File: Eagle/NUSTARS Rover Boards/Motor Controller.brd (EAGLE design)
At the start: 53.3 x 59.7 mm, 15 parts

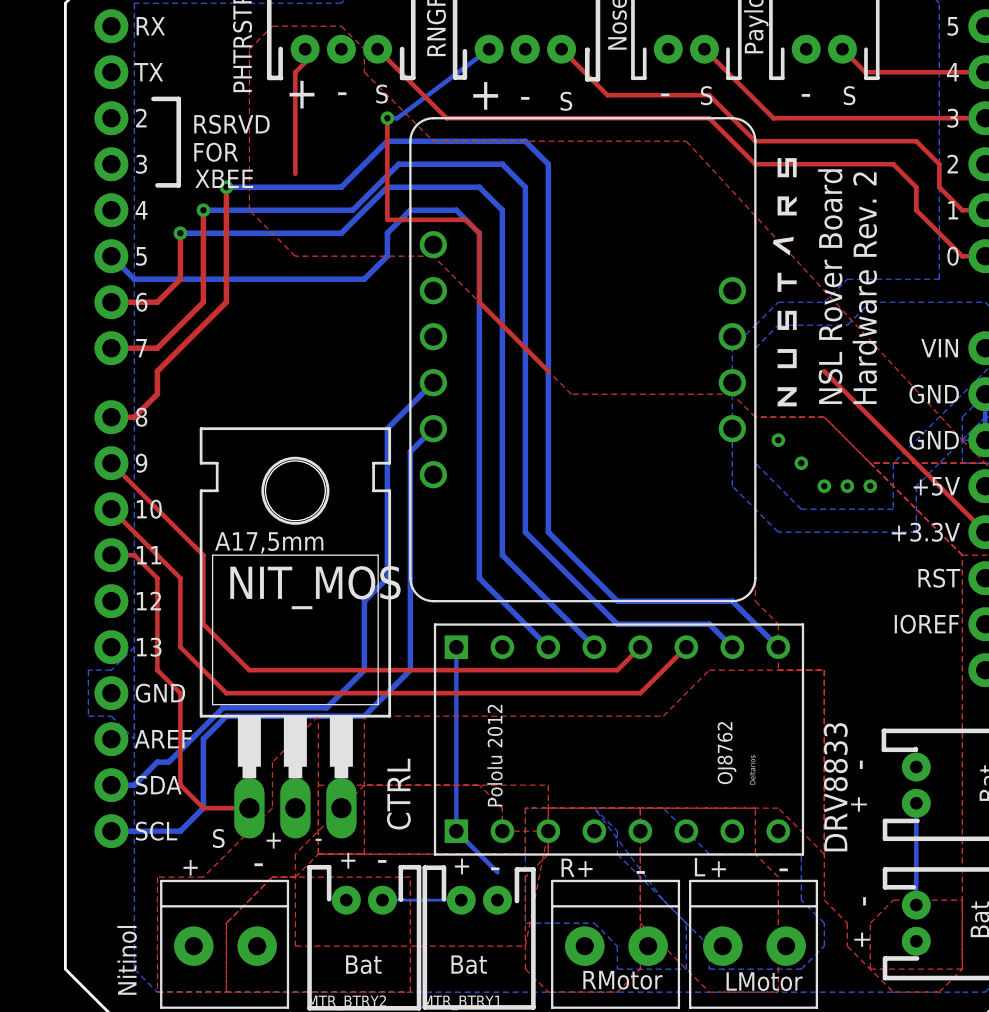
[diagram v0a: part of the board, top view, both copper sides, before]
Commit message: Add rover
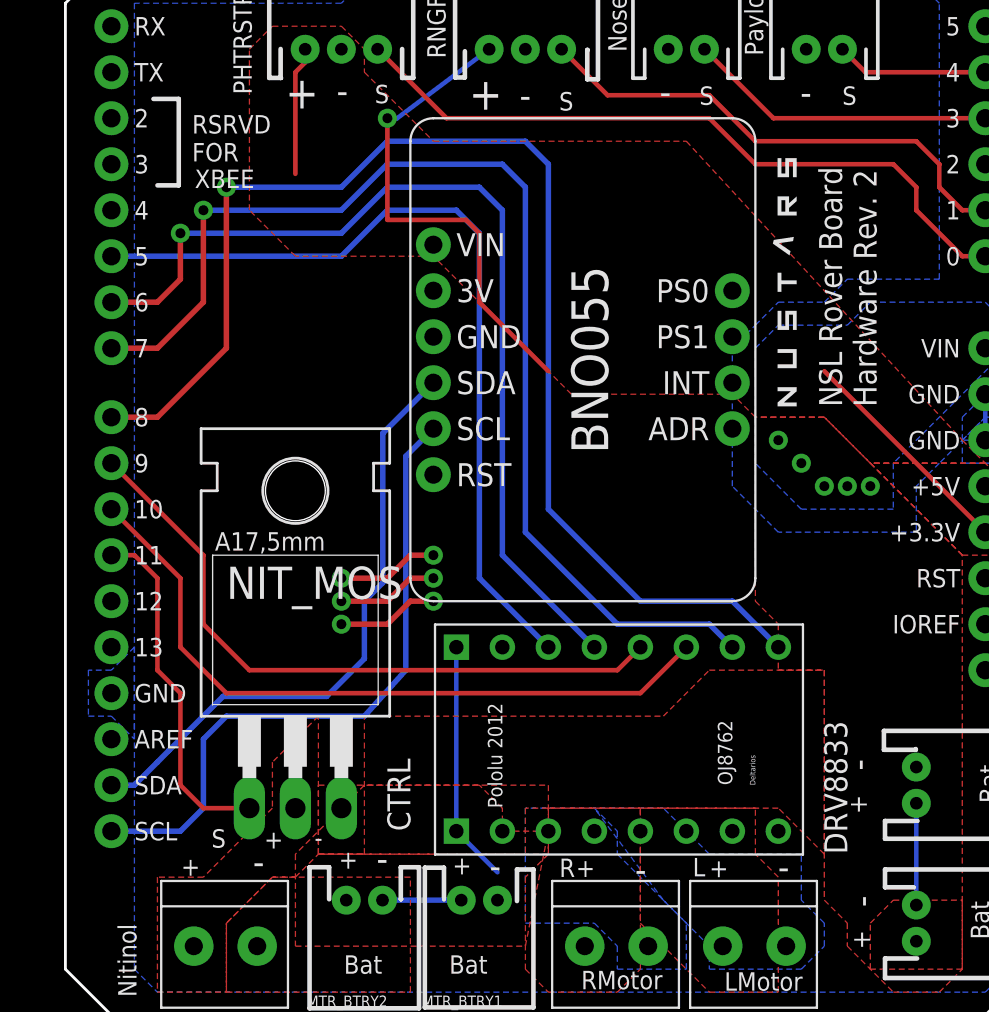
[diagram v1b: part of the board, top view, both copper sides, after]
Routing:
- net GND: track 15.9 -> 32.7 mm, vias 0 -> 6
- net D5: track 48.1 -> 46.3 mm
